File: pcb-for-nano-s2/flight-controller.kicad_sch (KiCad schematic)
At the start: 59 parts, among them J1 BM03B-SRSS-TBLFSN, J2 BM03B-SRSS-TBLFSN, J3 BM03B-SRSS-TBLFSN, J4 Conn_01x02, J5 Conn_ARM_JTAG_SWD_10, J6 Conn_01x02, Q1 Q_NMOS_GSD, Q2 Q_NMOS_GSD, U1 STM32G4A1KEU6, U2 ZOE-M8Q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

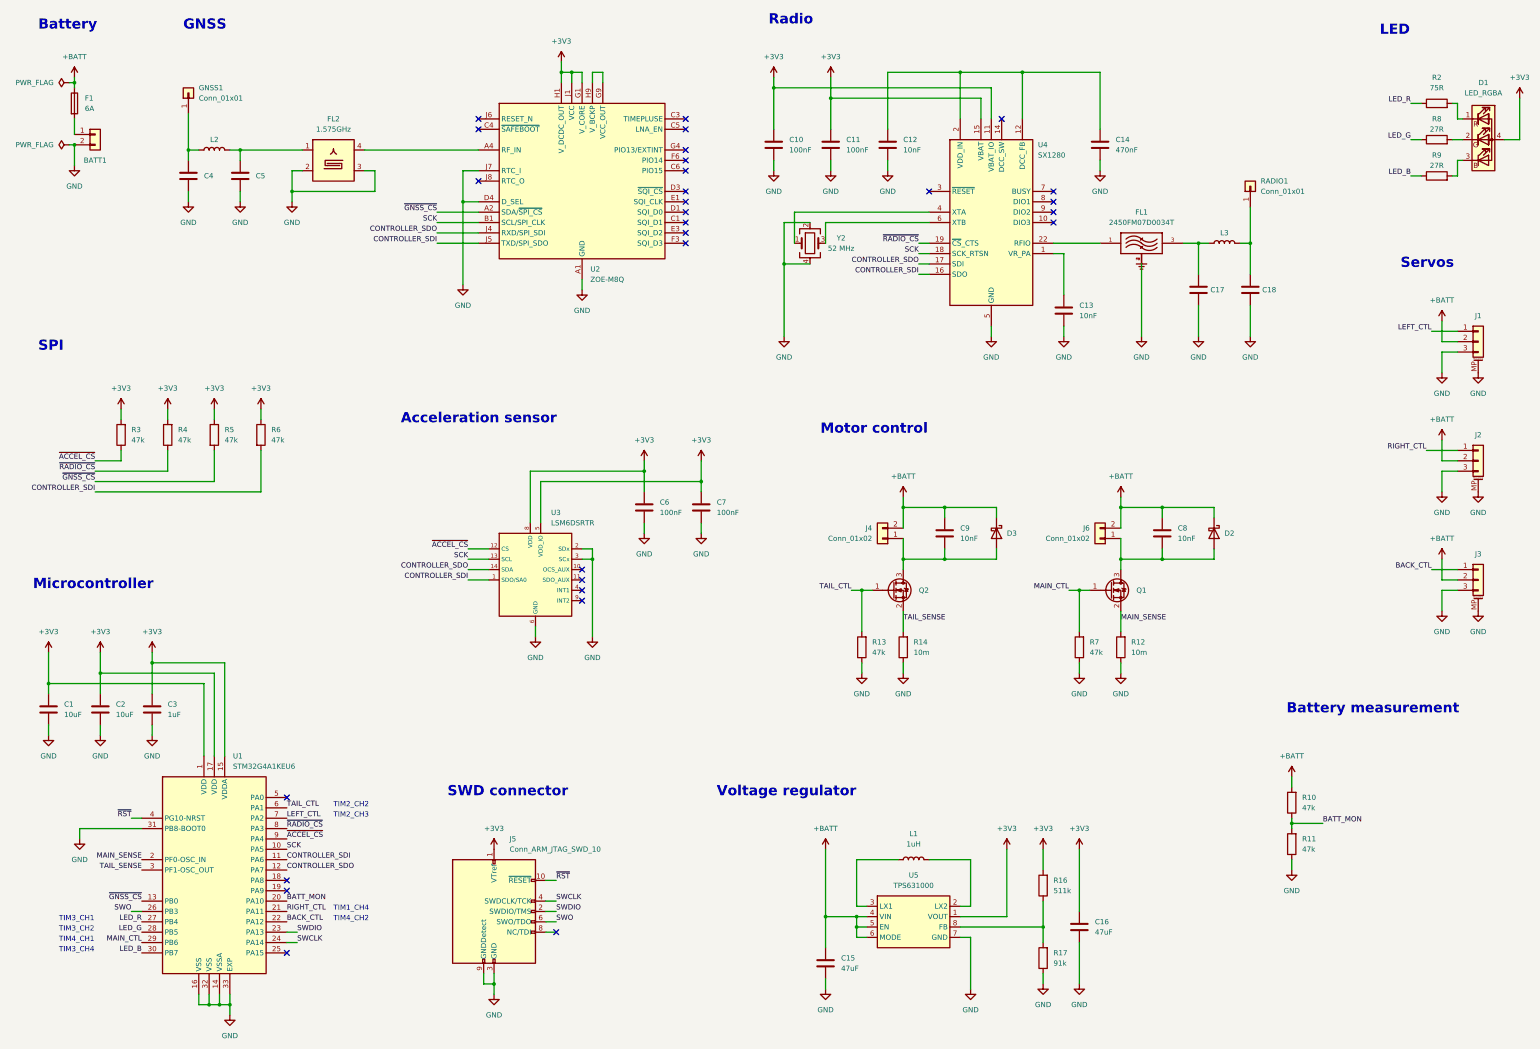
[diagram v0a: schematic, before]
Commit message: fix connections and add new ones in schematic
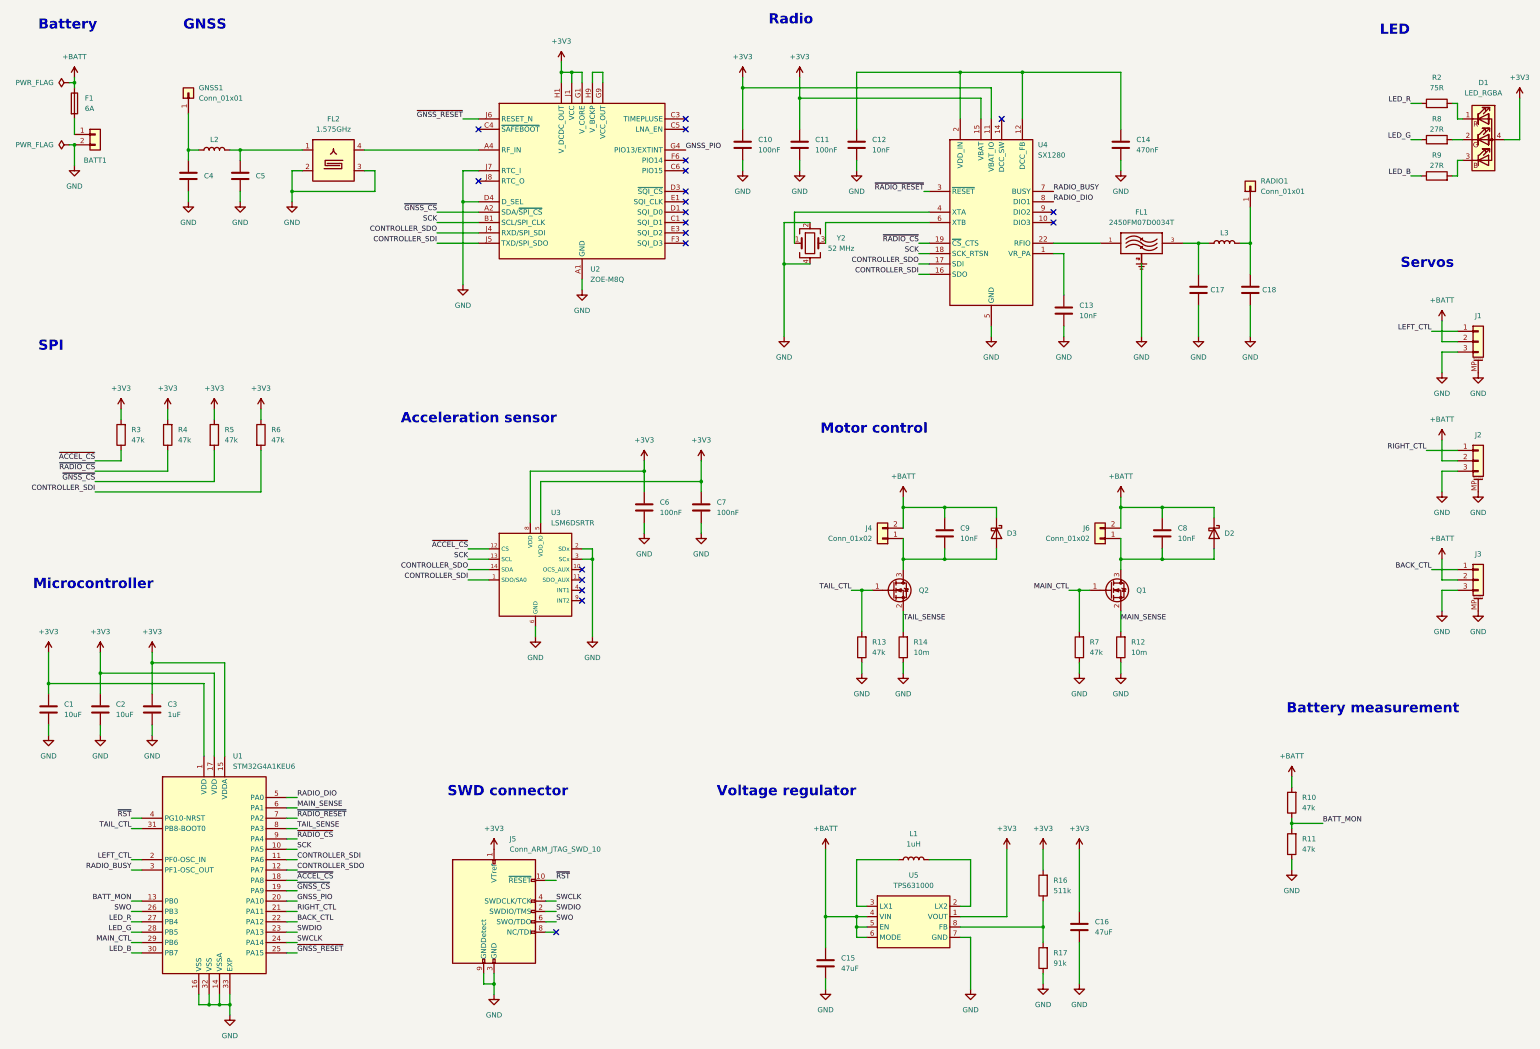
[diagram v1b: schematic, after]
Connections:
- net BATT_MON: now also U1.13 (PB0); no longer U1.20 (PA10)
- net GND: no longer U1.31 (PB8-BOOT0)
- net LEFT_CTL: now also U1.2 (PF0-OSC_IN); no longer U1.7 (PA2)
- net MAIN_SENSE: now also U1.6 (PA1); no longer U1.2 (PF0-OSC_IN)
- net TAIL_CTL: now also U1.31 (PB8-BOOT0); no longer U1.6 (PA1)
- net TAIL_SENSE: now also U1.8 (PA3); no longer U1.3 (PF1-OSC_OUT)
- net ~{ACCEL_CS}: now also U1.18 (PA8); no longer U1.9 (PA4)
- net ~{GNSS_CS}: now also U1.19 (PA9); no longer U1.13 (PB0)
- net ~{RADIO_CS}: now also U1.9 (PA4); no longer U1.8 (PA3)
- net ~{RADIO_RESET}: now reaches U4.3 (~{RESET})
- net ~{RADIO_RESET}: now also U1.7 (PA2)
- net RADIO_BUSY: now reaches U4.7 (BUSY)
- net RADIO_BUSY: now also U1.3 (PF1-OSC_OUT)
- net RADIO_DIO: now reaches U4.8 (DIO1)
- net RADIO_DIO: now also U1.5 (PA0)
- net GNSS_PIO: now reaches U2.G4 (PIO13/EXTINT)
- net GNSS_PIO: now also U1.20 (PA10)
- net ~{GNSS_RESET}: now reaches U2.J6 (RESET_N)
- net ~{GNSS_RESET}: now also U1.25 (PA15)
- no-connect marks 29 -> 20
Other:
- note removed: "TIM1_CH4"
- note removed: "TIM2_CH2"
- note removed: "TIM2_CH3"
- note removed: "TIM3_CH1"
- note removed: "TIM3_CH2"
- note removed: "TIM3_CH4"
- note removed: "TIM4_CH1"
- note removed: "TIM4_CH2"
- moved on the sheet: C10, C11, C12, C14
